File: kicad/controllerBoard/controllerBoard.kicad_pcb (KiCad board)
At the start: 4 copper layers, 150 x 150.6 mm, 763 parts, among them J1 Conn_02x20_Top_Bottom, J2 Conn_02x20_Top_Bottom, Q1 Q_PMOS_GSD, Q10 Q_NMOS_GSD, Q100 Q_NMOS_GSD, Q101 Q_PMOS_GSD, Q102 Q_NMOS_GSD, Q103 Q_PMOS_GSD, Q104 Q_NMOS_GSD, Q105 Q_PMOS_GSD, Q106 Q_NMOS_GSD, Q107 Q_PMOS_GSD, Q108 Q_NMOS_GSD, Q109 Q_PMOS_GSD, Q11 Q_PMOS_GSD, Q110 Q_NMOS_GSD, Q111 Q_PMOS_GSD, Q112 Q_NMOS_GSD, Q113 Q_PMOS_GSD, Q114 Q_NMOS_GSD, Q115 Q_PMOS_GSD, Q116 Q_NMOS_GSD, Q117 Q_PMOS_GSD, Q118 Q_NMOS_GSD, Q119 Q_PMOS_GSD, Q12 Q_NMOS_GSD, Q120 Q_NMOS_GSD, Q121 Q_PMOS_GSD, Q122 Q_NMOS_GSD, Q123 Q_PMOS_GSD, Q124 Q_NMOS_GSD, Q125 Q_PMOS_GSD, Q126 Q_NMOS_GSD, Q127 Q_PMOS_GSD, Q128 Q_NMOS_GSD, Q129 Q_PMOS_GSD, Q13 Q_PMOS_GSD, Q130 Q_NMOS_GSD, Q131 Q_PMOS_GSD, Q132 Q_NMOS_GSD, Q133 Q_PMOS_GSD, Q134 Q_NMOS_GSD, Q135 Q_PMOS_GSD, Q136 Q_NMOS_GSD, Q137 Q_PMOS_GSD, Q138 Q_NMOS_GSD, Q139 Q_PMOS_GSD, Q14 Q_PMOS_GSD, Q140 Q_NMOS_GSD, Q141 Q_PMOS_GSD, Q142 Q_NMOS_GSD, Q143 Q_PMOS_GSD, Q144 Q_NMOS_GSD, Q145 Q_PMOS_GSD, Q146 Q_NMOS_GSD, Q147 Q_PMOS_GSD, Q148 Q_NMOS_GSD, Q149 Q_PMOS_GSD, Q15 Q_PMOS_GSD, Q150 Q_NMOS_GSD, Q151 Q_PMOS_GSD, Q152 Q_NMOS_GSD, Q153 Q_PMOS_GSD, Q154 Q_NMOS_GSD, Q155 Q_PMOS_GSD, Q156 Q_NMOS_GSD, Q157 Q_PMOS_GSD, Q158 Q_NMOS_GSD, Q159 Q_PMOS_GSD, Q16 Q_NMOS_GSD, Q160 Q_NMOS_GSD, Q161 Q_PMOS_GSD, Q162 Q_NMOS_GSD, Q163 Q_PMOS_GSD, Q164 Q_NMOS_GSD, Q165 Q_PMOS_GSD, Q166 Q_NMOS_GSD, Q167 Q_PMOS_GSD, Q168 Q_NMOS_GSD, Q169 Q_PMOS_GSD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

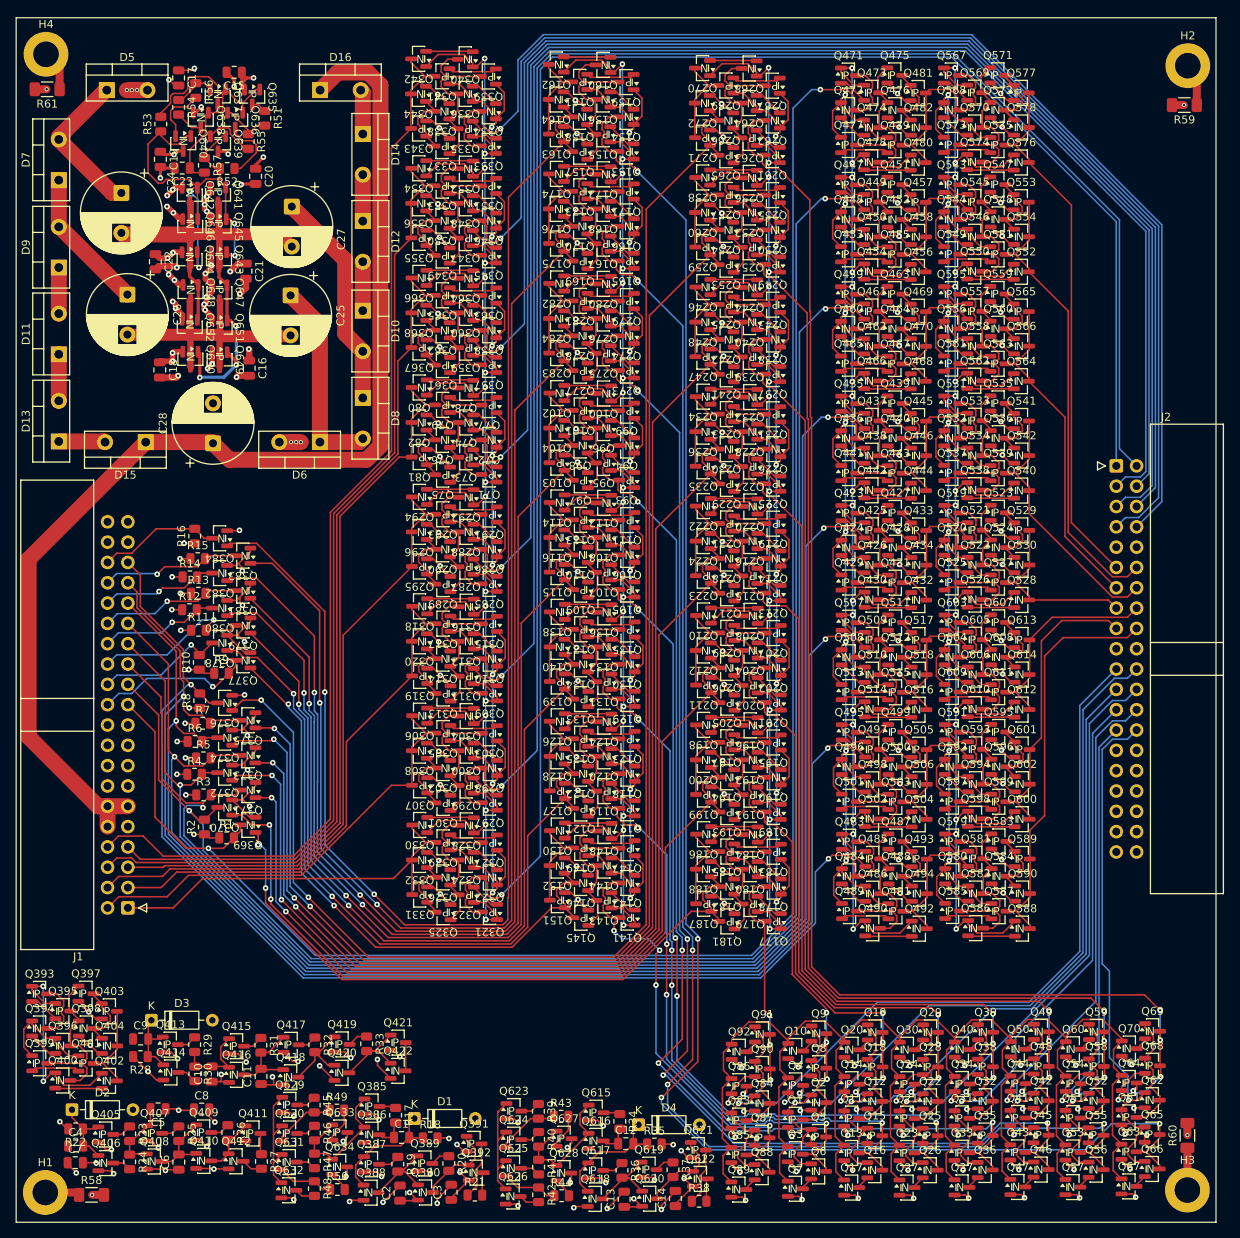
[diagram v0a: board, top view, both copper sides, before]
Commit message: Add breakout board through holes on main ram board
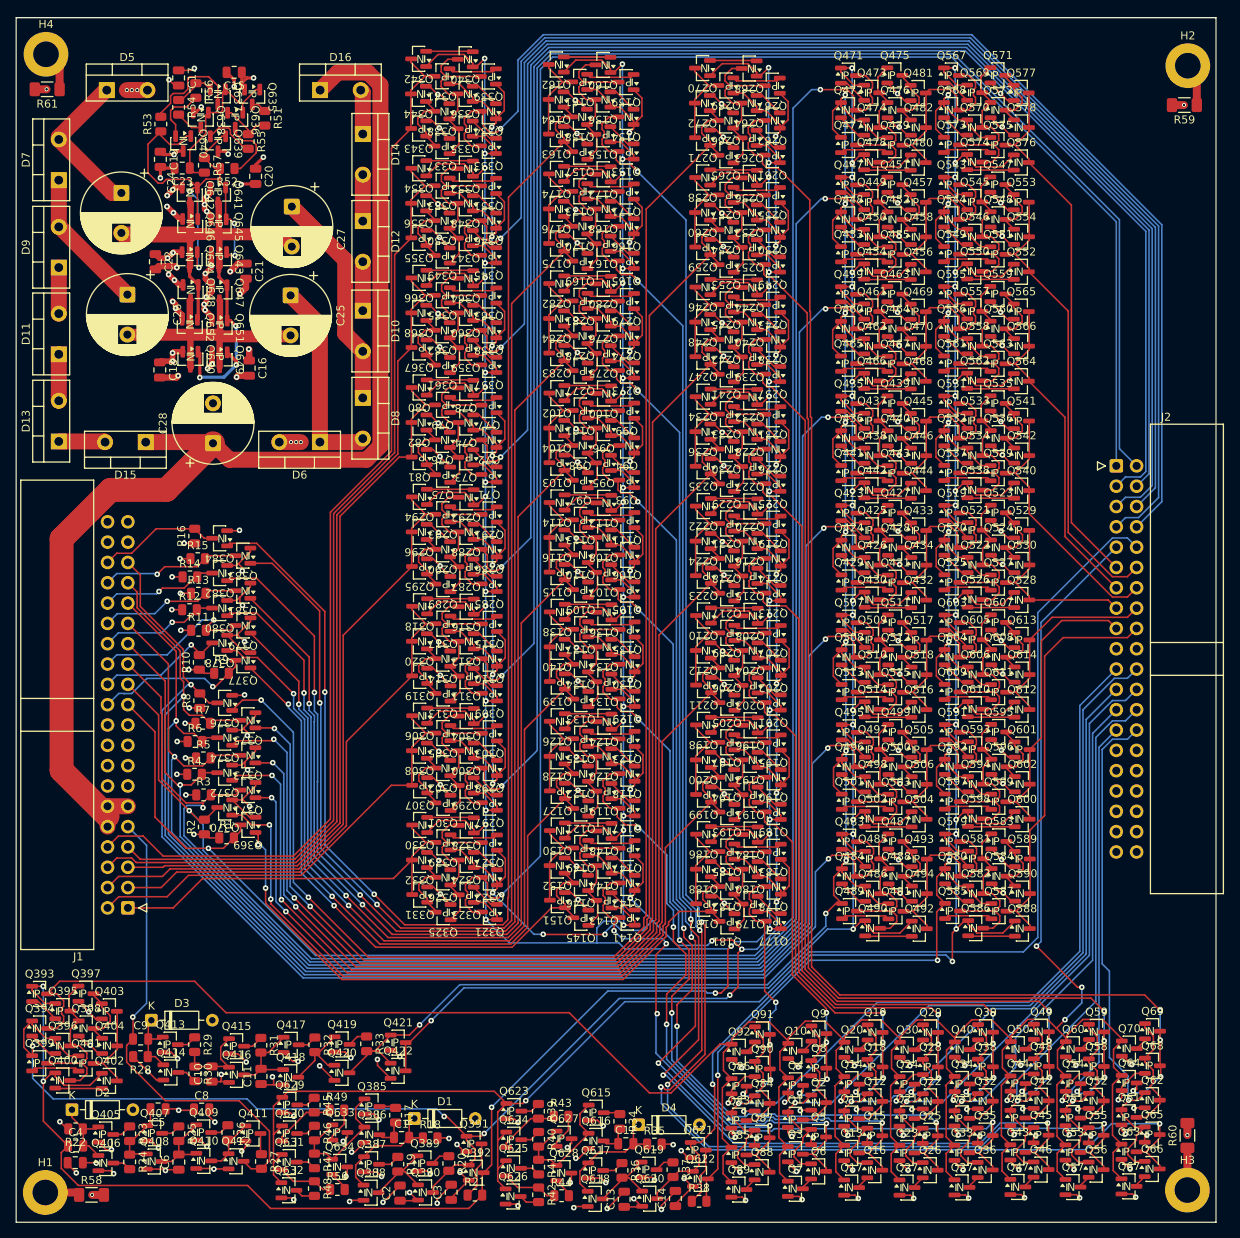
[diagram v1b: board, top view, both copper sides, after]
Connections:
- J2 pad 19: unconnected-(J2-Pin_19-Pad19) -> GND
- J2 pad 20: unconnected-(J2-Pin_20-Pad20) -> GND
- J2 pad 29: unconnected-(J2-Pin_29-Pad29) -> +5V
- J2 pad 30: unconnected-(J2-Pin_30-Pad30) -> +5V
- J2 pad 31: unconnected-(J2-Pin_31-Pad31) -> +5V
- J2 pad 32: unconnected-(J2-Pin_32-Pad32) -> +5V
- J2 pad 33: unconnected-(J2-Pin_33-Pad33) -> +5V
- J2 pad 34: unconnected-(J2-Pin_34-Pad34) -> +5V
- J2 pad 35: unconnected-(J2-Pin_35-Pad35) -> GND
- J2 pad 36: unconnected-(J2-Pin_36-Pad36) -> GND
- J2 pad 37: unconnected-(J2-Pin_37-Pad37) -> GND
- J2 pad 38: unconnected-(J2-Pin_38-Pad38) -> GND
- J2 pad 39: unconnected-(J2-Pin_39-Pad39) -> GND
- J2 pad 40: unconnected-(J2-Pin_40-Pad40) -> GND
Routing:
- net /OP_{in}: track 235.6 -> 398.3 mm, vias 0 -> 3
- net /~{EN_{input}}: track 707.4 -> 868.8 mm, vias 50 -> 53
- net /CLK: track 29.0 -> 190.3 mm, vias 0 -> 1
- net /EN_{input}: track 662.5 -> 821.1 mm, vias 24 -> 32
- net /R_PULSE: track 223.9 -> 288.0 mm, vias 8 -> 10
- net /~{R_PULSE}: track 229.5 -> 291.3 mm, vias 16 -> 17
- net /WL_PULSE: track 2.62 -> 60.6 mm, vias 0 -> 1
- net /8DLATCH4/EN: track 215.7 -> 271.8 mm, vias 8 -> 10
- net /8DLATCH4/~{EN}: track 236.6 -> 289.5 mm, vias 16 -> 18
- net +10V: track 146.6 -> 151.2 mm
- net GND: track 343.1 -> 347.4 mm, vias 120 -> 122
- net /~{BL}_{nctrl ncl 1}: track 74.8 -> 76.8 mm
- net /~{BL}_{nctrl ncl 7}: track 207.9 -> 209.8 mm
- net /~{BL}_{nctrl ncl 0}: track 55.9 -> 57.8 mm
- net /~{BL}_{nctrl ncl 2}: track 95.0 -> 96.8 mm
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- added copper zone on In2.Cu, net +5V
- added copper zone on In1.Cu, net GND
